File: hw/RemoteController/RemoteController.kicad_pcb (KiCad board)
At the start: 4 copper layers, 100 x 75 mm, 138 parts, among them J1 Conn_01x04_Pin, J2 Conn_01x04_Pin, J4 BWSMA-KWE-Z3.5*4.2, SW2 ST-0-102-A01-T000-LF, SW6 TS-1088-AR02016, SW7 TS-1088-AR02016, SW8 TS-1088-AR02016, SW9 TS-1088-AR02016, U1 LM358, U10 H3-TCD-12-222X+, U11 LM358, U13 nRF52810-QFxx, U14 LM358, U15 LM358, U16 H3-TCD-12-222X+, U17 AD8313xRM, U18 LM358, U2 TPS562200, U3 SPF5043Z, U4 MICRF220AYQS, U5 XA17-G4K, U6 MAX7044AKA, U8 AD8313xRM, U9 GVA-63, Y1 32 MHz, Y2 L327S13CU11L, Y4 13.56 MHz, Y5 32.768 KHz

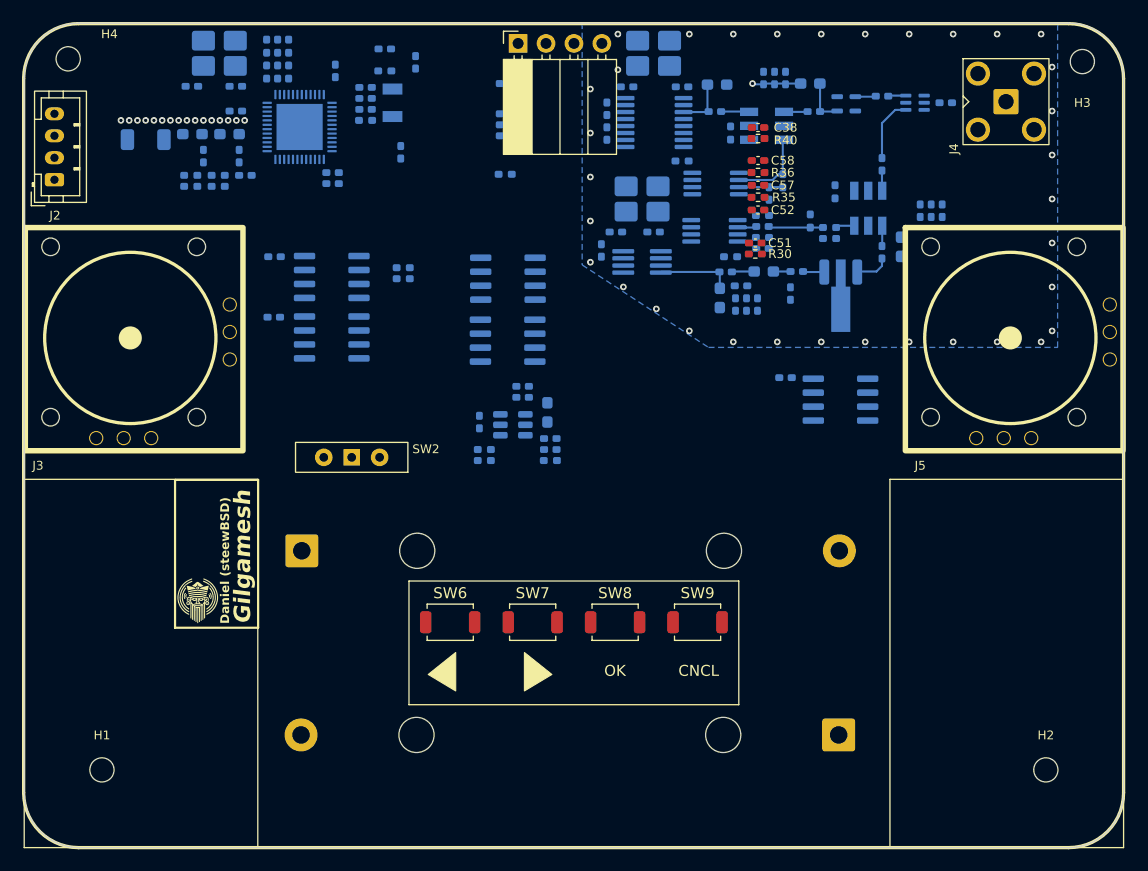
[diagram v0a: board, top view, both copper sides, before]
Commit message: remote_ctrl: advance routing
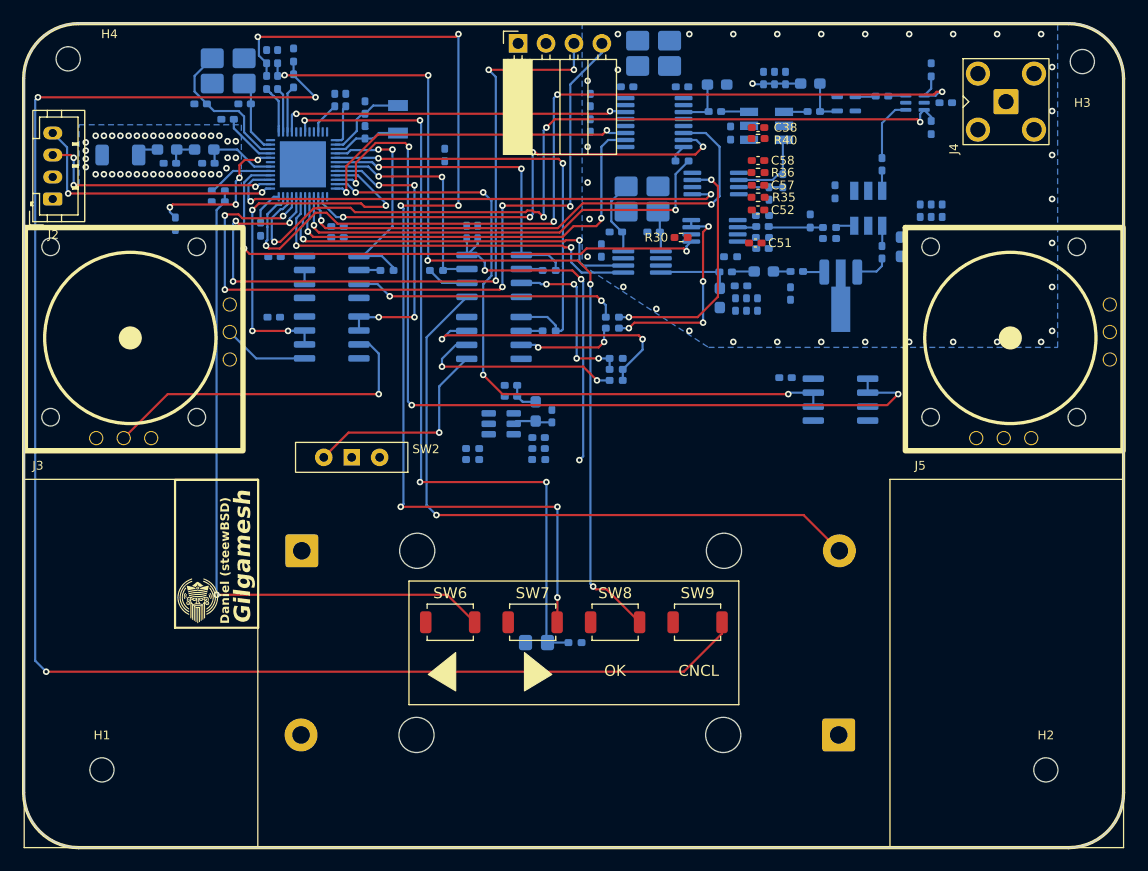
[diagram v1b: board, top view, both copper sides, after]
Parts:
- added R20: 50K, Resistor_SMD:R_0402_1005Metric_Pad0.72x0.64mm_HandSolder, B.Cu at (117.0, 76.8)
- added R21: 5K, Resistor_SMD:R_0402_1005Metric_Pad0.72x0.64mm_HandSolder, B.Cu at (145.6, 114.3)
- added TH1: B59721A0100A062, Resistor_SMD:R_0805_2012Metric_Pad1.20x1.40mm_HandSolder, B.Cu at (142.1, 114.3)
- moved R32 65.7 mm to (178.0, 62.2), turned to -90 degrees
- moved R31 65.0 mm to (178.0, 67.5), turned to 90 degrees
- moved R29 25.4 mm to (143.2, 86.0)
- moved R33 24.4 mm to (149.3, 90.5)
- moved R8 24.4 mm to (149.3, 88.5)
- moved R9 24.4 mm to (149.3, 89.5)
- moved R38 19.3 mm to (149.0, 84.8)
- moved R11 18.7 mm to (133.0, 80.5), turned to 0 degrees
- moved C16 18.7 mm to (136.8, 77.0), turned to 90 degrees
- moved R10 17.4 mm to (143.2, 80.5), turned to 0 degrees
- moved R28 17.1 mm to (149.0, 85.8)
- moved C11 16.1 mm to (135.8, 77.0)
- moved C20 7.74 mm to (109.2, 76.2), turned to -90 degrees
- moved R30 6.91 mm to (155.2, 77.5), turned to 180 degrees
- moved C14 6.62 mm to (143.5, 93.8)
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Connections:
- R40 pad 1: /Radio/~{EN_RXSAMPLE} -> /~{EN_RXSAMPLE}
- U13 pad 17: unconnected-(U13-P0.14-Pad17) -> /DATAOUT
- U13 pad 18: /DATAOUT -> /TXDATA
- U13 pad 19: /TXDATA -> /TXCLK
- U13 pad 20: /TXCLK -> /OLED_SCL
- U13 pad 21: /OLED_SCL -> /OLED_SDA
- U13 pad 22: /OLED_SDA -> /RF_SEL0
- U13 pad 23: /RF_SEL0 -> /RF_SEL1
- U13 pad 24: unconnected-(U13-P0.21/~{RESET}-Pad24) -> Net-(U13-P0.21/~{RESET})
- U13 pad 27: /RF_SEL1 -> /~{EN_RXSAMPLE}
- U13 pad 43: unconnected-(U13-P0.31/AIN7-Pad43) -> Net-(U13-P0.31/AIN7)
- U17 pad 5: /Radio/~{EN_RXSAMPLE} -> /~{EN_RXSAMPLE}
- U6 pad 5: /Radio/TXCLK -> /TXCLK
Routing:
- net Net-(R15-Pad2): track 0.00 -> 145.9 mm, vias 0 -> 3
- net Net-(R13-Pad2): track 0.00 -> 95.5 mm, vias 0 -> 7
- net /RF_SEL1: track 0.00 -> 84.0 mm, vias 0 -> 4
- net /POTSW2Y: track 0.00 -> 82.1 mm, vias 0 -> 4
- net Net-(R12-Pad2): track 0.00 -> 81.2 mm, vias 0 -> 5
- net /RF_SEL0: track 0.00 -> 76.3 mm, vias 0 -> 4
- net Net-(U13-P0.31/AIN7): track 0.00 -> 72.6 mm, vias 0 -> 4
- net /OLED_SDA: track 0.00 -> 69.4 mm, vias 0 -> 6
- net /OLED_SCL: track 0.00 -> 66.8 mm, vias 0 -> 6
- net /POTSW2X: track 0.00 -> 63.1 mm, vias 0 -> 4
- net Net-(R14-Pad2): track 0.00 -> 61.6 mm, vias 0 -> 1
- net /VBAT1: track 0.00 -> 59.7 mm, vias 0 -> 1
- net /~{EN_TXSAMPLE}: track 0.00 -> 50.5 mm, vias 0 -> 2
- net /RX_SQUELCH: track 0.00 -> 48.6 mm, vias 0 -> 2
- net /~{EN_RXSAMPLE}: track 0.00 -> 47.6 mm, vias 0 -> 2
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
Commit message: remote_ctrl: finish preliminary routing
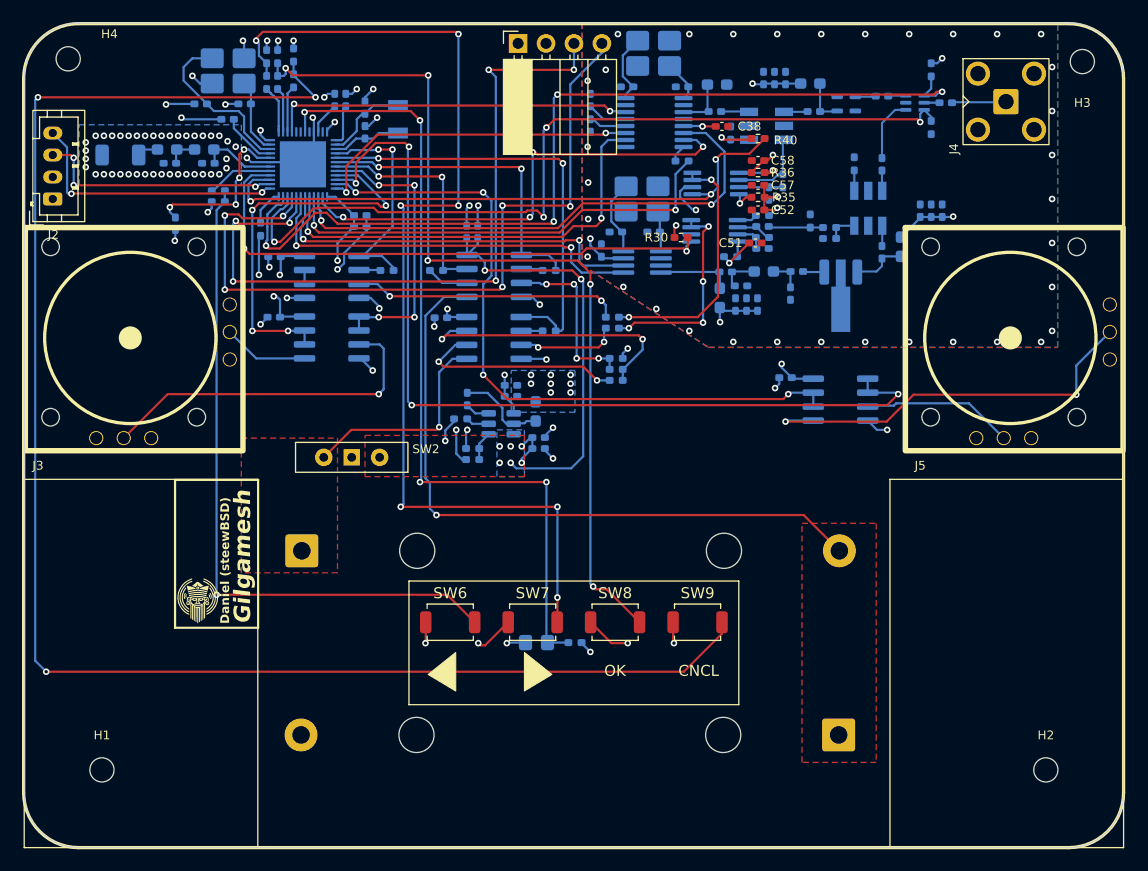
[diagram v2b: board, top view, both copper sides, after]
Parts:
- moved C54 14.8 mm to (133.4, 84.8), turned to 0 degrees
- moved R1 8.00 mm to (135.2, 94.0), turned to 0 degrees
- moved C14 7.85 mm to (135.8, 92.2), turned to 90 degrees
- moved C38 3.28 mm to (159.0, 67.4)
- moved R4 3.09 mm to (171.0, 70.8)
- moved C23 2.30 mm to (126.1, 75.5)
- moved C24 2.30 mm to (126.1, 76.5)
- turned C51 to 180 degrees
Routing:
- net +3V0: track 7.32 -> 82.3 mm, vias 1 -> 34
- net GND: track 0.15 -> 72.9 mm, vias 75 -> 110
- net /XPOTSW2X: track 0.00 -> 37.0 mm, vias 0 -> 2
- net /XPOTSW2Y: track 0.00 -> 13.8 mm
- net /VBAT2: track 31.7 -> 45.0 mm, vias 3 -> 9
- net /~{EN_RXSAMPLE}: track 47.6 -> 56.4 mm, vias 2 -> 3
- net Net-(U4-RO2): track 0.00 -> 6.47 mm
- net Net-(J4-In): track 0.14 -> 4.95 mm
- net Net-(U2-SW): track 3.63 -> 8.30 mm
- net Net-(R36-Pad2): track 0.00 -> 4.02 mm, vias 0 -> 1
- net Net-(U4-RO1): track 0.00 -> 3.81 mm
- net Net-(U4-CAGC): track 0.00 -> 3.68 mm
- net Net-(U4-CTH): track 0.00 -> 3.45 mm
- net Net-(U8-INLO): track 0.00 -> 2.78 mm
- net Net-(U2-VFB): track 0.00 -> 2.66 mm
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- added copper zone on B.Cu, net +3V0
- added copper zone on F.Cu, net /VBAT1
- added copper zone on B.Cu, net /VBAT2
- added copper zone on F.Cu, net /VBAT2
- added copper zone on F.Cu, net GND
- added copper zone on F.Cu, net Net-(BT1-+)

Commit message: remote_ctrl: final touches
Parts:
- moved H1 12.6 mm to (114.4, 130.4)
- moved H2 12.5 mm to (176.8, 130.4)
- moved H4 0.74 mm to (99.0, 61.8)
- moved J5 0.65 mm to (183.8, 72.4)
- moved J3 0.40 mm to (104.8, 72.3)
- moved H3 0.39 mm to (192.0, 61.8)
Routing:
- net GND: vias 110 -> 168
- net +3V0: vias 34 -> 35

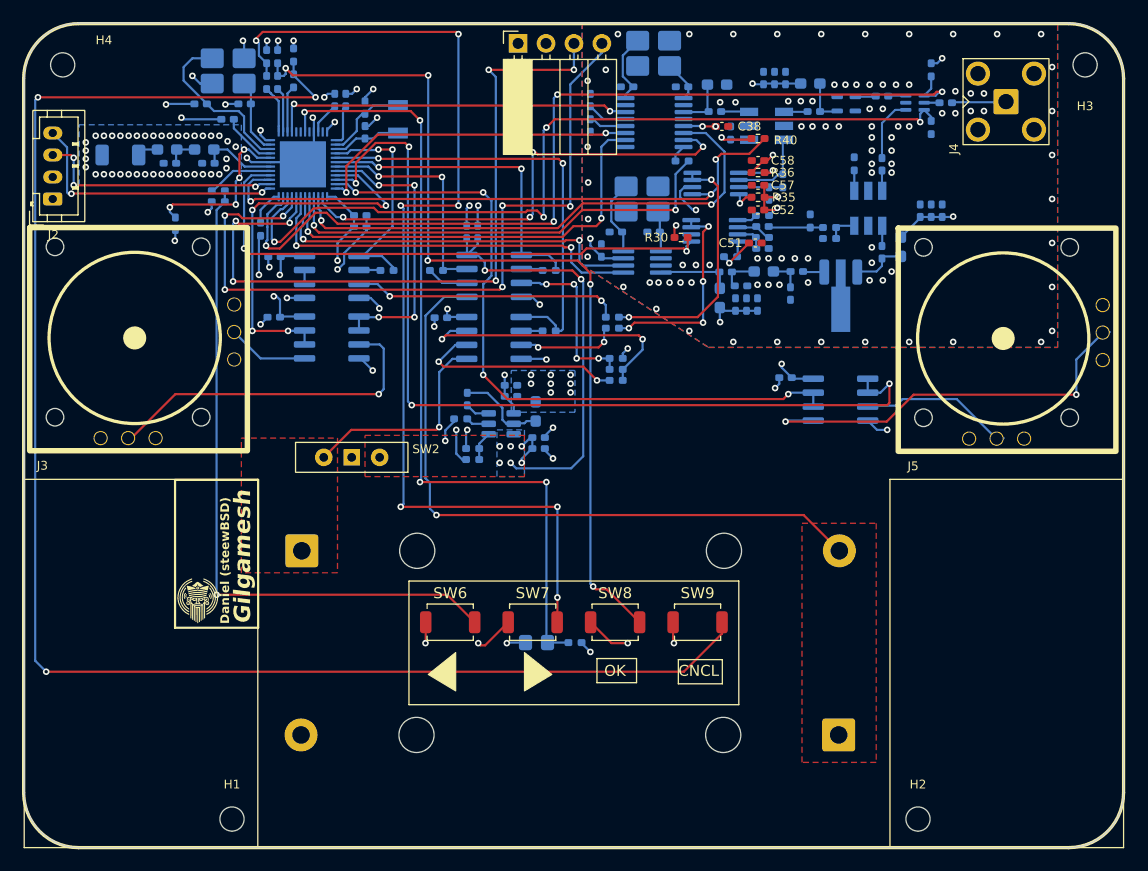
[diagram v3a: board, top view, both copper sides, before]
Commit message: remote_ctrl: change logdet to AD8314 and battery holder to SMD
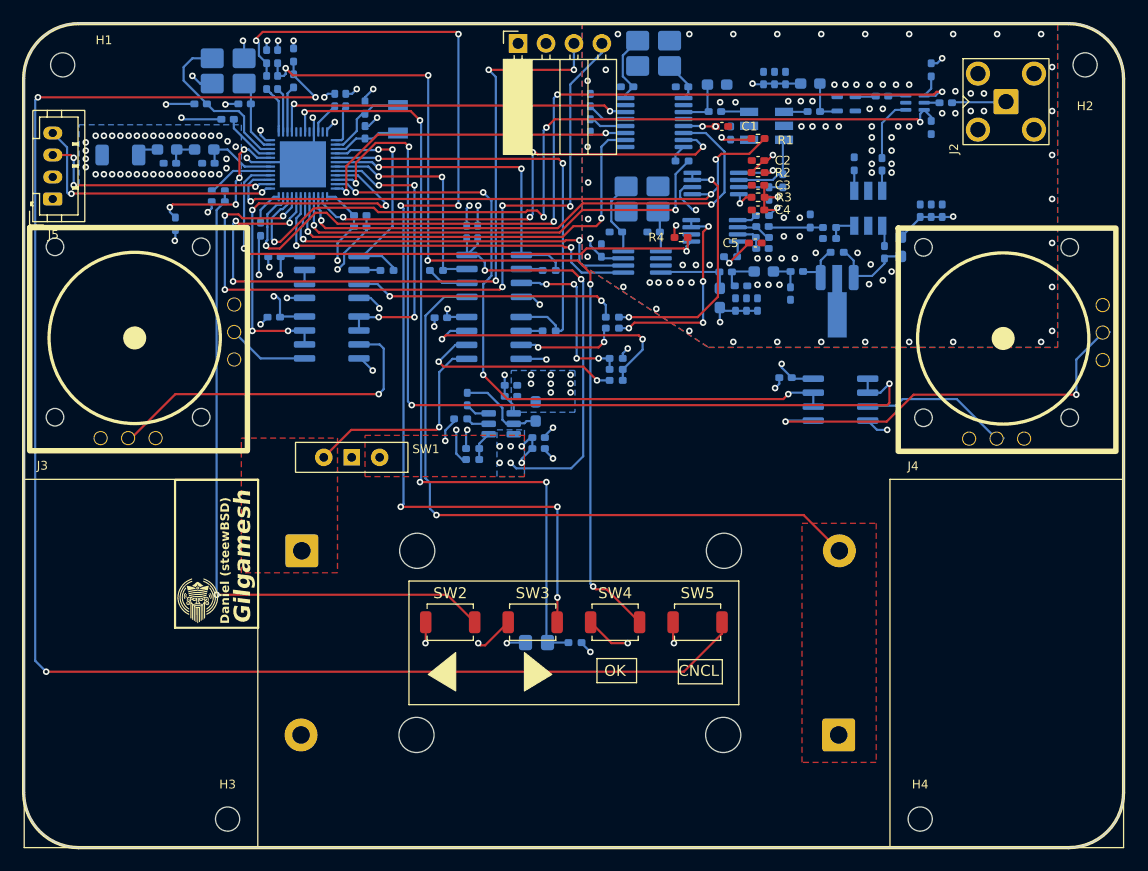
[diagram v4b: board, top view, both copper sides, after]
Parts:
- added R40: 0R, Resistor_SMD:R_0402_1005Metric_Pad0.72x0.64mm_HandSolder, B.Cu at (169.4, 78.8)
- moved U12 0.60 mm to (169.4, 83.6)
- moved H3 0.40 mm to (114.0, 130.4)
- moved C41 0.22 mm to (173.8, 78.8)
- moved H4 0.20 mm to (177.0, 130.4)
- renumbered C38 to C1, C17 to C10, C34 to C11, C39 to C12, C19 to C13, C22 to C14, C27 to C15, C5 to C16, C6 to C17, C7 to C18, C60 to C19, C58 to C2, C35 to C20, C33 to C22, C8 to C23, C32 to C24, C3 to C25, C4 to C26, C59 to C27, C44 to C28, C45 to C29, C57 to C3, C46 to C30, C23 to C31, C20 to C32, C53 to C33, C24 to C34, C2 to C35, C1 to C36, C16 to C37, C11 to C38, C48 to C39, C52 to C4, C37 to C40, C47 to C41, C61 to C42, C36 to C44, C31 to C45, C30 to C46, C26 to C47, C18 to C48, C15 to C49, C51 to C5, C54 to C50, C55 to C51, C56 to C52, C13 to C53, C12 to C54, C14 to C55, C9 to C56, C10 to C57, C62 to C6, C64 to C7, C63 to C8, C25 to C9, H4 to H1, H3 to H2, H1 to H3, H2 to H4, J4 to J2, J5 to J4, J2 to J5, L9 to L1, L5 to L2, L2 to L3, L10 to L4, L8 to L5, L4 to L6, L3 to L7, L1 to L8, R40 to R1, R18 to R10, R17 to R11, R31 to R12, R34 to R13, R41 to R14, R4 to R15, R37 to R16, R16 to R17, R14 to R18, R26 to R19, R36 to R2, R5 to R20, R6 to R21, R20 to R22, R27 to R23, R7 to R24, R10 to R26, R11 to R27, R39 to R28, R38 to R29, R35 to R3, R28 to R30, R29 to R31, R8 to R32, R9 to R33, R33 to R34, R1 to R35, R2 to R36, R3 to R37, R21 to R38, R30 to R4, R15 to R5, R12 to R6, R13 to R7, R32 to R8, R19 to R9, SW2 to SW1, SW6 to SW2, SW7 to SW3, SW8 to SW4, SW9 to SW5, U5 to U1, U11 to U10, U18 to U11, U9 to U12, U1 to U13, U2 to U16, U3 to U2, U4 to U3, U16 to U4, U13 to U5, U17 to U6, U10 to U7, U6 to U9, Y2 to Y1, Y1 to Y2, Y5 to Y3
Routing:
- net Net-(C41-Pad1): track 4.97 -> 8.26 mm
- net Net-(C43-Pad2): track 1.95 -> 4.87 mm
- net GND: vias 168 -> 171
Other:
- board text added: "NM"

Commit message: remote_ctrl: finish new layout with components changed
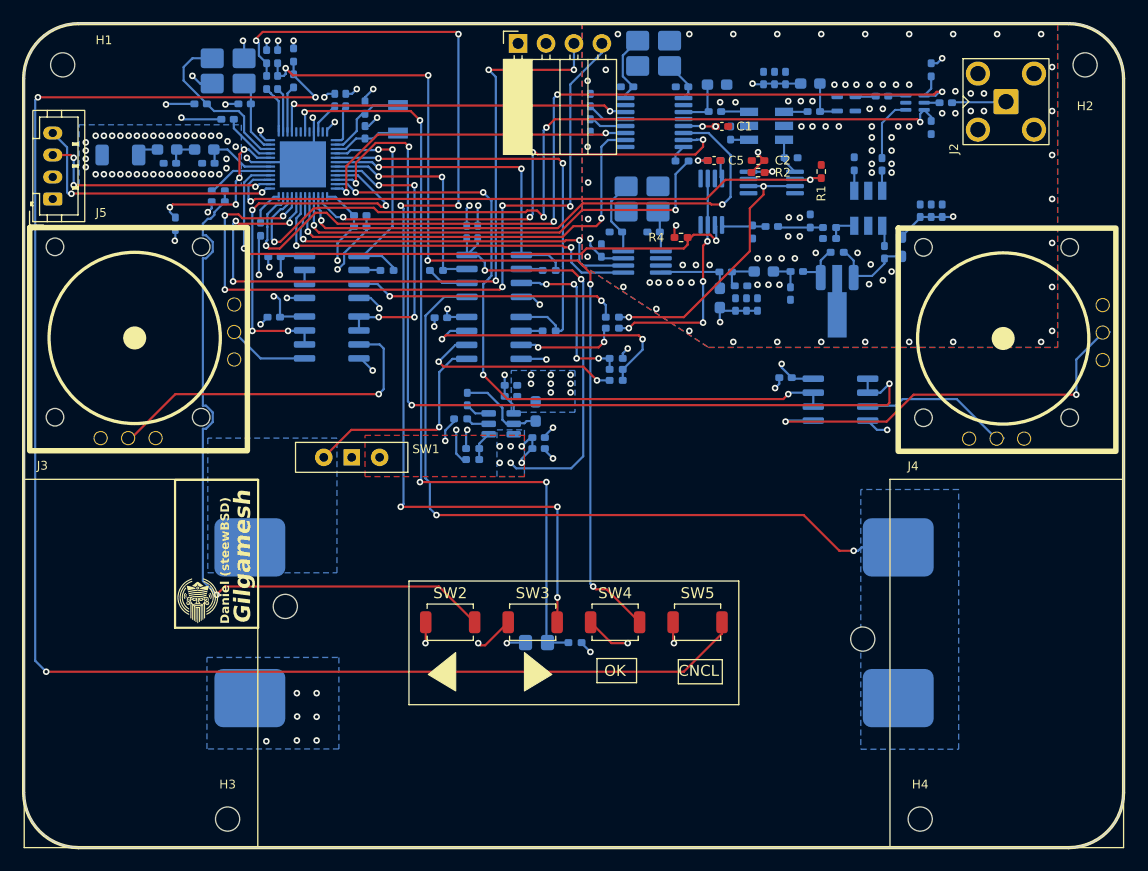
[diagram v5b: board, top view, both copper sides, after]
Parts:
- removed C27, C39: 680P, Capacitor_SMD:C_0402_1005Metric_Pad0.74x0.62mm_HandSolder
- removed C3, C4: 100N, Capacitor_SMD:C_0402_1005Metric_Pad0.74x0.62mm_HandSolder
- removed R16: 53R6, Resistor_SMD:R_0402_1005Metric_Pad0.72x0.64mm_HandSolder
- removed R19, R3: 10R, Resistor_SMD:R_0402_1005Metric_Pad0.72x0.64mm_HandSolder
- removed U6, U8: AD8313xRM, Package_SO:MSOP-8_3x3mm_P0.65mm
- added R39: 52R3, Resistor_SMD:R_0402_1005Metric_Pad0.72x0.64mm_HandSolder, B.Cu at (165.2, 70.2)
- added U17: AD8314RM, Package_SO:MSOP-8_3x3mm_P0.65mm, B.Cu at (158.0, 74.2)
- added U18: AD8314RM, Package_SO:MSOP-8_3x3mm_P0.65mm, B.Cu at (163.5, 72.5)
- BT1, BT2: footprint Battery:BatteryHolder_Bulgin_BX0034_1xAAA -> steew:BH-AAA-B5BA021
- R23: value 53R6 -> 52R3
- moved BT1 25.0 mm to (145.7, 106.7)
- moved BT2 24.7 mm to (145.3, 118.4)
- moved R25 8.88 mm to (158.2, 70.5), turned to 0 degrees
- moved C5 8.39 mm to (158.2, 70.5)
- moved R1 6.49 mm to (168.0, 71.5), turned to 90 degrees
- moved R23 1.03 mm to (161.8, 77.0), turned to -90 degrees
- moved C33 0.85 mm to (163.5, 76.5)
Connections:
- net /~{EN_RXSAMPLE} renamed /EN_RXSAMPLE
- net /~{EN_TXSAMPLE} renamed /EN_TXSAMPLE
- C33 pad 2: Net-(U8-INHI) -> Net-(U17-RFIN)
- R1 pad 2: +3V0 -> GND
- R23 pad 1: Net-(U8-INLO) -> Net-(U17-RFIN)
- R23 pad 2: Net-(U8-INHI) -> GND
- R25 pad 1: Net-(R25-Pad1) -> +3V0
- R25 pad 2: +3V0 -> Net-(U17-VPOS)
- R4 pad 2: +3V0 -> GND
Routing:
- net +3V0: track 82.3 -> 70.9 mm, vias 35 -> 31
- net /VBAT1: track 61.0 -> 66.5 mm, vias 1 -> 2
- net Net-(U17-RFIN): track 0.00 -> 4.01 mm
- net Net-(U6-INLO): track 4.01 -> 0.00 mm
- net Net-(R17-Pad2): track 61.6 -> 65.5 mm
- net Net-(U18-RFIN): track 7.40 -> 3.48 mm
- net Net-(U8-INHI): track 3.31 -> 0.00 mm
- net /EN_TXSAMPLE: track 51.8 -> 54.8 mm
- net Net-(U8-INLO): track 2.78 -> 0.00 mm
- net GND: track 72.9 -> 70.3 mm, vias 171 -> 178
- net Net-(R3-Pad1): track 2.16 -> 0.00 mm, vias 1 -> 0
- net Net-(U17-VSET): track 19.1 -> 21.1 mm
- net Net-(U18-VSET): track 23.1 -> 25.0 mm
- net Net-(R19-Pad2): track 1.83 -> 0.00 mm
- net Net-(U17-VPOS): track 0.00 -> 1.69 mm
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- added copper zone on B.Cu, net /VBAT1
- added copper zone on B.Cu, net Net-(BT1-+)
- removed copper zone on F.Cu, net /VBAT1
- removed copper zone on F.Cu, net Net-(BT1-+)

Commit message: remote_ctrl: finish teardrops and DRC
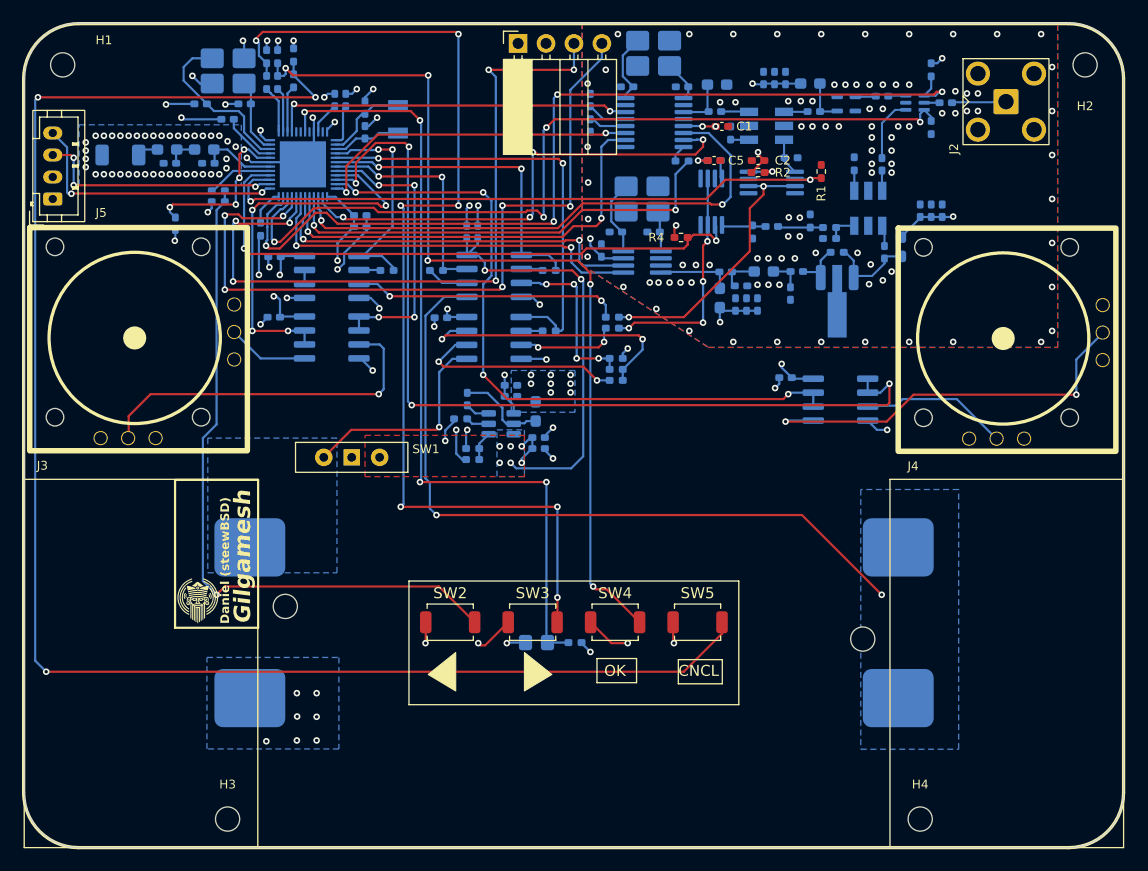
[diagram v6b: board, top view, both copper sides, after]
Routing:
- net GND: track 70.3 -> 68.0 mm
- net Net-(R17-Pad2): track 65.5 -> 63.2 mm
- net +3V0: track 70.9 -> 69.3 mm
- net Net-(U5-XC2): track 6.90 -> 6.02 mm
- net /XPOTSW2Y: track 14.1 -> 13.3 mm
- net /XPOTSW1Y: track 31.6 -> 32.4 mm
- net Net-(C43-Pad2): track 4.87 -> 4.12 mm
- net Net-(U7-IN): track 2.19 -> 1.45 mm
- net Net-(AE1-PCB_Trace): track 1.92 -> 1.21 mm
- net Net-(C41-Pad1): track 8.26 -> 7.61 mm
- net /XPOTSW2X: track 37.3 -> 36.8 mm
